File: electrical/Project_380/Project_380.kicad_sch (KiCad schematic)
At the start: 2 parts, among them J14 UART_to_USB, U2 ESP32-WROOM

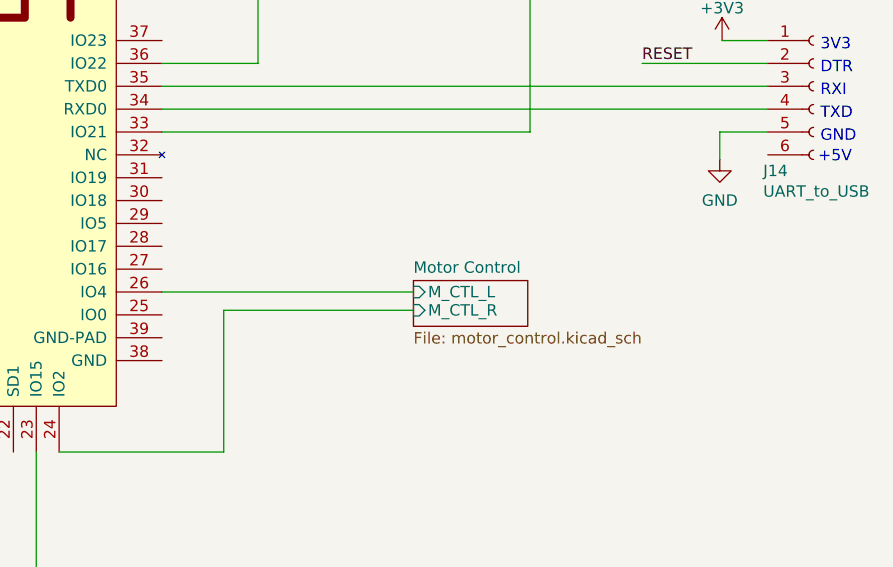
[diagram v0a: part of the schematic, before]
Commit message: added downforce motor control pin
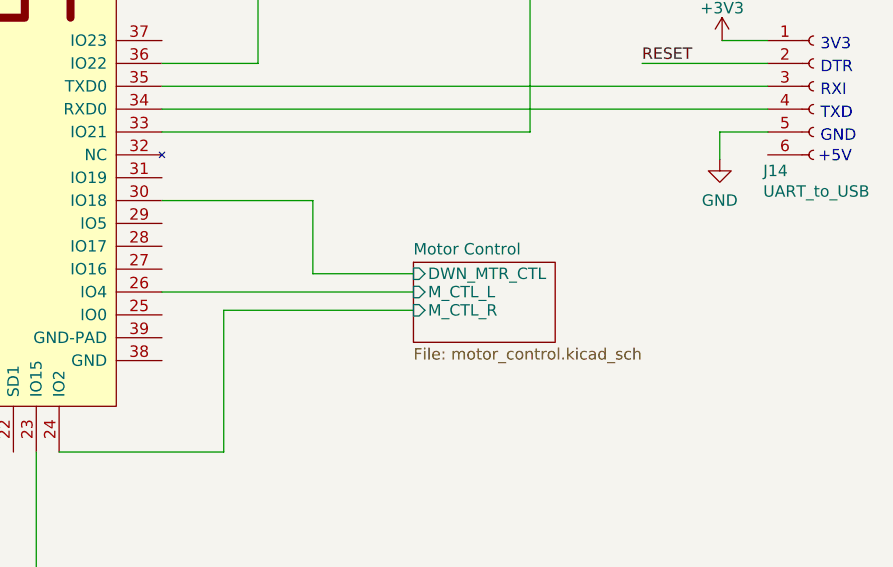
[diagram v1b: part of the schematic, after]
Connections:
- net Motor Control/DWN_MTR_CTL: now reaches U2.30 (IO18)
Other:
- sheet Motor Control ports: added DWN_MTR_CTL; removed none
- title: (none) -> Top Level
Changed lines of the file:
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@@
 (kicad_sch (version 20211123) (generator eeschema)
   (paper "A4")
+  (title_block
+    (title "Top Level")
+    (date "2022-02-03")
+    (rev "1.0")
+  )
   (junction (at 94.742 116.078) (diameter 0) (color 0 0 0 0)
   )
@@
     (stroke (width 0) (type default) (color 0 0 0 0))
   )
+  (wire (pts (xy 145.796 87.122) (xy 145.796 95.25))
+    (stroke (width 0) (type default) (color 0 0 0 0))
+  )
   (wire (pts (xy 169.926 38.862) (xy 169.926 79.502))
     (stroke (width 0) (type default) (color 0 0 0 0))
@@
     (stroke (width 0) (type default) (color 0 0 0 0))
   )
+  (wire (pts (xy 145.796 95.25) (xy 156.972 95.25))
+    (stroke (width 0) (type default) (color 0 0 0 0))
+  )
   (wire (pts (xy 139.7 38.862) (xy 139.7 71.882))
+    (stroke (width 0) (type default) (color 0 0 0 0))
+  )
+  (wire (pts (xy 129.032 87.122) (xy 145.796 87.122))
     (stroke (width 0) (type default) (color 0 0 0 0))
   )
@@
     (pin "1")
   )
-  (sheet (at 156.972 96.012) (size 12.7 5.08) (fields_autoplaced)
+  (sheet (at 156.972 93.98) (size 15.748 8.89) (fields_autoplaced)
     (stroke (width 0.1524) (type solid) (color 0 0 0 0))
     (fill (color 0 0 0 0.0000))
-    (property "Sheet name" "Motor Control" (id 0) (at 156.972 95.3004 0)
+    (property "Sheet name" "Motor Control" (id 0) (at 156.972 93.2684 0)
       (effects (font (size 1.27 1.27)) (justify left bottom))
     )
-    (property "Sheet file" "motor_control.kicad_sch" (id 1) (at 156.972 101.6766 0)
+    (property "Sheet file" "motor_control.kicad_sch" (id 1) (at 156.972 103.4546 0)
       (effects (font (size 1.27 1.27)) (justify left top))
     )
@@
       (effects (font (size 1.27 1.27)) (justify left))
     )
+    (pin "DWN_MTR_CTL" input (at 156.972 95.25 180)
+      (effects (font (size 1.27 1.27)) (justify left))
+    )

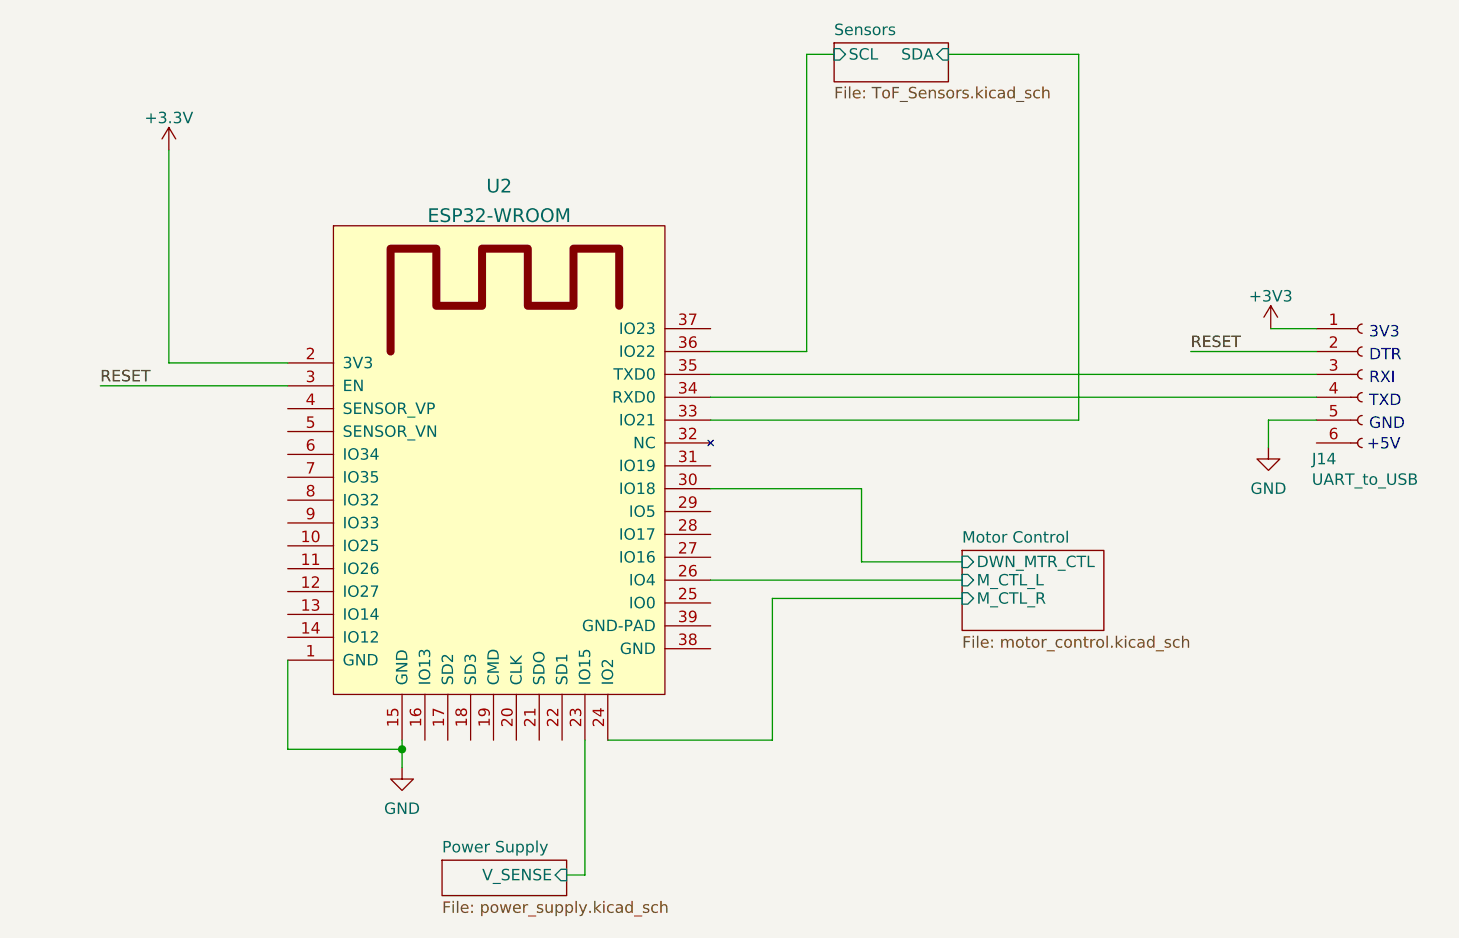
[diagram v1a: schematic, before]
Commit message: added reset functionality, created schematic pdfs
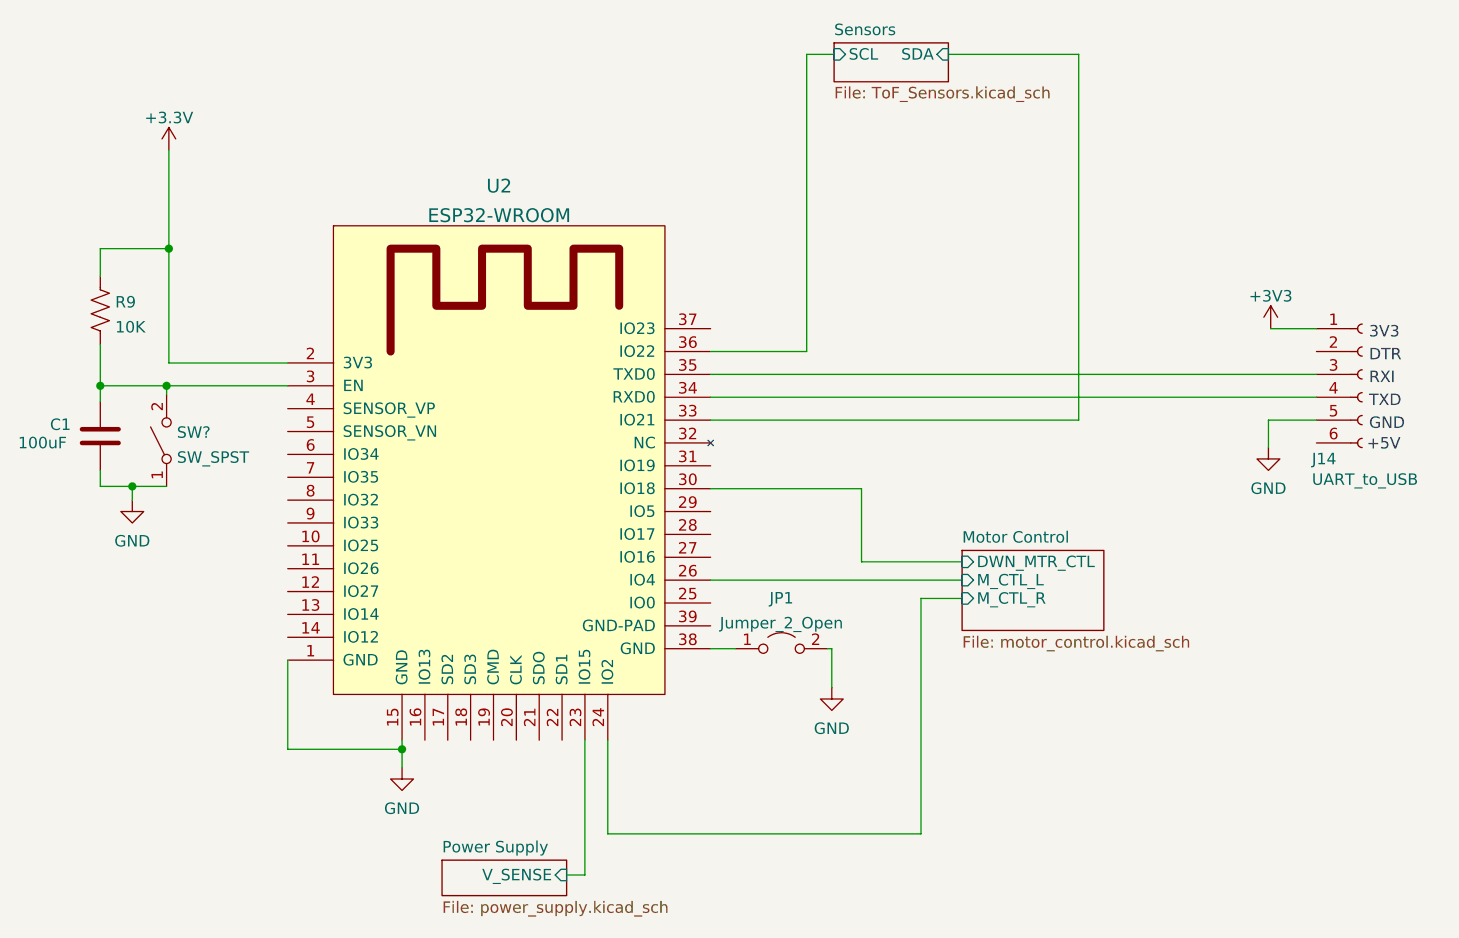
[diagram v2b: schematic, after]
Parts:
- added C1: 100uF, symbol Device:C
- added JP1: Jumper_2_Open, symbol Jumper:Jumper_2_Open
- added R9: 10K, symbol Device:R_US
- added SW?: SW_SPST, symbol Switch:SW_SPST
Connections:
- net +3V3: now also R9.1
- net GND: now also C1.2, JP1.2 (B), SW?.1 (A)
- net at U2.38 (GND): now also JP1.1 (A)
- net RESET: no longer names the net of U2.3 (EN)
- net RESET: now also C1.1, R9.2, SW?.2 (B); no longer J14.2 (Pin_2)

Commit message: added motor controller
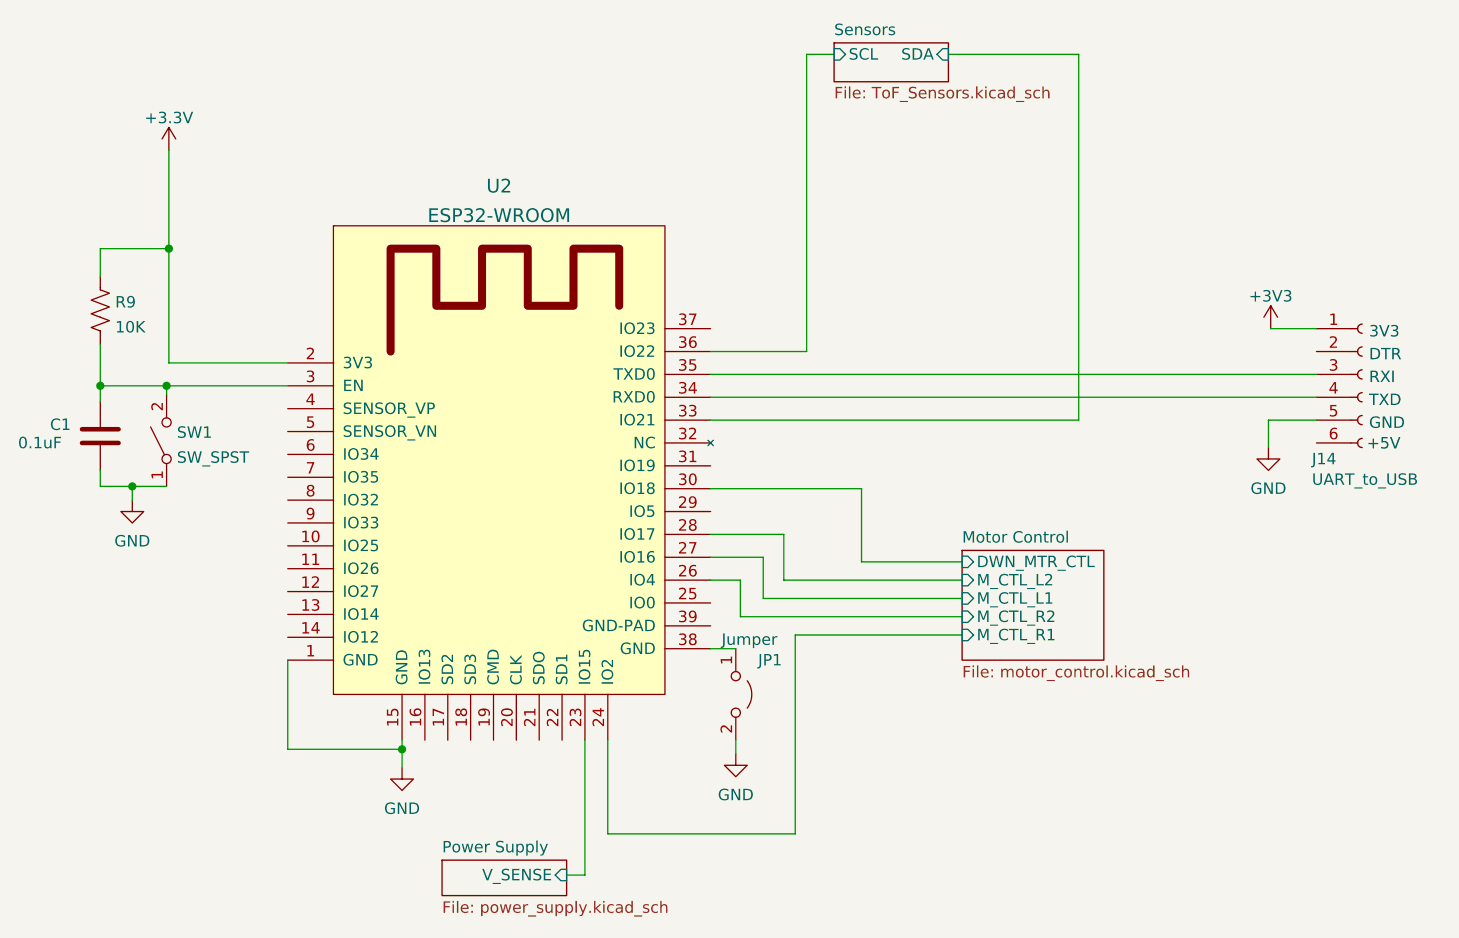
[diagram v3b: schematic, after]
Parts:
- C1: value 100uF -> 0.1uF
- JP1: value Jumper_2_Open -> Jumper
- R9: footprint (none) -> Resistor_SMD:R_0603_1608Metric
- gave numbers to parts that had none: 1
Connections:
- net Motor Control/M_CTL_L1: now reaches U2.27 (IO16)
- net Motor Control/M_CTL_L2: now reaches U2.28 (IO17)
- net Motor Control/M_CTL_L renamed Motor Control/M_CTL_R2
- net Motor Control/M_CTL_R renamed Motor Control/M_CTL_R1
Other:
- sheet Motor Control ports: added M_CTL_L1, M_CTL_L2, M_CTL_R1, M_CTL_R2; removed M_CTL_L, M_CTL_R
- moved on the sheet: JP1
